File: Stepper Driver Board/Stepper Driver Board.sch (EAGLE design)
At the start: 23 parts, among them IC1 DRV8825PWP

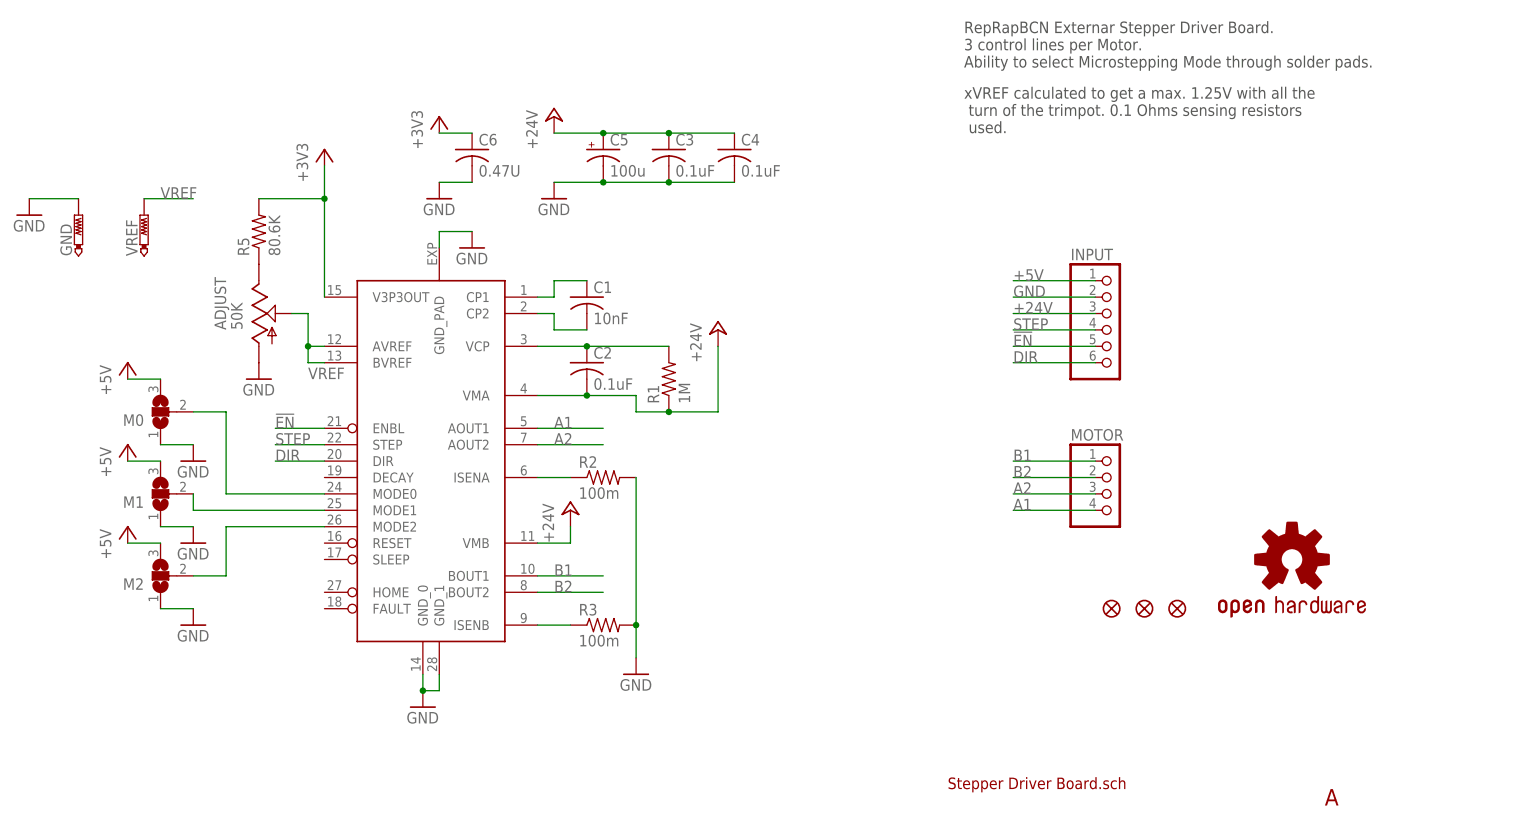
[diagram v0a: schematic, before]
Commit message: The new REV_B has been shipped to production
New MainBoard Design, new Stepper drivers and new Extruder Board.
We also added many new components and configurations
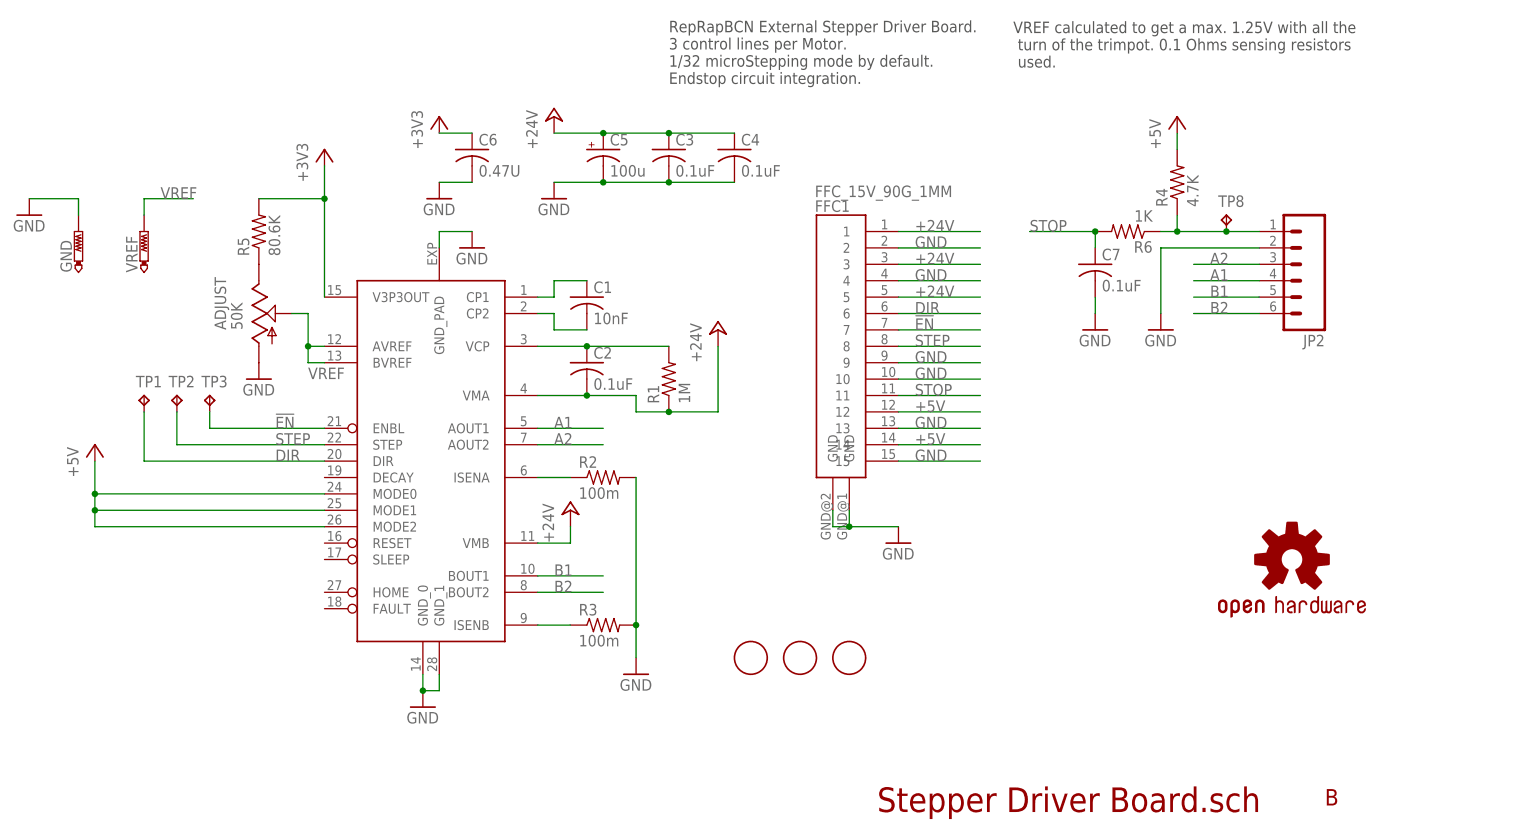
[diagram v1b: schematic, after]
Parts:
- removed FID1, FID2, FID3: FIDUCIAL1X2, SparkFun-Aesthetics:FIDUCIAL1X2
- removed INPUT: (no value), pinhead:PINHD-1X6/90
- removed M0, M1, M2: (no value), jumper:SJ2W
- removed MOTOR: (no value), pinhead:PINHD-1X4/90
- added C7: 0.1uF, rcl:C-USC0805
- added FFC1: FFC_15V_90G_1MM, MarcEagleParts:FFC_15V_90G_1MM
- added JP2: (no value), SparkFun-Connectors:M06SMD
- added R4: 4.7K, rcl:R-US_R0805
- added R6: 1K, rcl:R-US_R0805
- added TP1, TP2, TP3, TP8: TPB1,27, testpad:TPB1,27
- added U$2, U$3, U$4: FIDUCIAL, adafruit:FIDUCIAL
- C5: device rcl:CPOL-USUD-8X10 -> rcl:CPOL-USUD-6,3X7,7
- GND, VREF: value TESTPAD_PTR1TP20SQ -> PTR1TP12R; device SAV MK-I:TESTPAD_PTR1TP20SQ -> testpad:PTR1TP12R; OC_FARNELL unknown -> (none)
- R2, R3: device rcl:R-US_R0805 -> rcl:R-US_R1210
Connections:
- removed net N$10: IC1.MODE1, M1.2
- removed net N$13: IC1.MODE2, M2.2
- removed net N$9: IC1.MODE0, M0.2
- new net N$25: JP2.1, R4.1, R6.1, TP8.TP
- new net N$30: JP2.2
- new net STOP: C7.1, FFC1.11, R6.2
- net !EN: now also FFC1.7, TP3.TP; no longer INPUT.5
- net +24V: now also FFC1.1, FFC1.3, FFC1.5; no longer INPUT.3
- net +5V: now also FFC1.12, FFC1.14, IC1.MODE0, IC1.MODE1, IC1.MODE2, R4.2; no longer INPUT.1, M0.3, M1.3, M2.3
- net A1: now also JP2.4; no longer MOTOR.4
- net A2: now also JP2.3; no longer MOTOR.3
- net B1: now also JP2.5; no longer MOTOR.1
- net B2: now also JP2.6; no longer MOTOR.2
- net DIR: now also FFC1.6, TP1.TP; no longer INPUT.6
- net GND: now also C7.2, FFC1.10, FFC1.13, FFC1.15, FFC1.2, FFC1.4, FFC1.9, FFC1.GND@1, FFC1.GND@2; no longer INPUT.2, M0.1, M1.1, M2.1
- net STEP: now also FFC1.8, TP2.TP; no longer INPUT.4
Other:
- note added: "B"
- note added: "RepRapBCN External Stepper Driver Board. 3 control lines per Motor. 1/32 microStepping mode by default. Endstop circuit integration."
- note added: "VREF calculated to get a max. 1.25V with all the turn of the trimpot. 0.1 Ohms sensing resistors used."
- note removed: "A"
- note removed: "RepRapBCN Externar Stepper Driver Board. 3 control lines per Motor. Ability to select Microstepping Mode through solder pads."
- note removed: "xVREF calculated to get a max. 1.25V with all the turn of the trimpot. 0.1 Ohms sensing resistors used."
- moved on the sheet: GND, VREF

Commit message: BCN3D Electronics REV.E tested and manufactured
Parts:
- removed FFC1: FFC_15V_90G_1MM, MarcEagleParts:FFC_15V_90G_1MM
- removed GND, VREF: PTR1TP12R, testpad:PTR1TP12R
- removed JP2: (no value), SparkFun-Connectors:M06SMD
- removed LOGO1: OSHW-LOGOL, SparkFun-Aesthetics:OSHW-LOGOL
- removed TP8: TPB1,27, testpad:TPB1,27
- added C8: 0.1uF, rcl:C-USC0805
- added FFC2: FFC_15V_90G_1MM, MarcEagleParts:FFC_15V_90G_1MM
- added MOTOR: (no value), MarcEagleParts:M06
- added SMAEX: (no value), SparkFun-Connectors:M03PTH
- added STOP: TPB1,27, testpad:TPB1,27
- added STOP1: (no value), adafruit:JST_2PIN-THM-RA
- added USTEP: (no value), jumper:SJ2W
- !EN, DIR, STEP, U$2, U$3, U$4: OC_FARNELL (none) -> unknown
- C3: value 0.1uF -> 100n
- R4: MF (none) -> PANASONIC ELECTRONIC COMPONENTS; MPN (none) -> ERJP06F4701V; OC_FARNELL (none) -> 1750763
- R6: MF (none) -> BOURNS; MPN (none) -> CR0805-JW-102ELF; OC_FARNELL (none) -> 2008389
- renumbered TP1 to DIR, TP2 to STEP, TP3 to !EN
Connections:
- removed net N$30: JP2.2
- new net N$4: IC1.MODE0, USTEP.2
- net !EN: now also FFC2.9; no longer FFC1.7
- net +24V: now also C8.1, FFC2.11, FFC2.13, FFC2.15; no longer FFC1.1, FFC1.3, FFC1.5
- net +5V: now also FFC2.2, FFC2.4, IC1.RESET, IC1.SLEEP, SMAEX.1, USTEP.3; no longer FFC1.12, FFC1.14, IC1.MODE0, IC1.MODE1
- net A1: now also MOTOR.6; no longer JP2.4
- net A2: now also MOTOR.4; no longer JP2.3
- net B1: now also MOTOR.1; no longer JP2.5
- net B2: now also MOTOR.3; no longer JP2.6
- net DIR: now also FFC2.7; no longer FFC1.6
- net GND: now also C8.2, FFC2.1, FFC2.12, FFC2.14, FFC2.3, FFC2.6, FFC2.8, FFC2.GND@1, FFC2.GND@2, IC1.MODE1, MOTOR.2, MOTOR.5, SMAEX.2, STOP1.2, USTEP.1; no longer FFC1.10, FFC1.13, FFC1.15, FFC1.2, FFC1.4, FFC1.9, FFC1.GND@1, FFC1.GND@2, GND.TP
- net N$25: now also STOP1.1; no longer JP2.1, TP8.TP
- net STEP: now also FFC2.10; no longer FFC1.8
- net STOP: now also FFC2.5, SMAEX.3, STOP.TP; no longer FFC1.11
- net VREF: no longer VREF.TP
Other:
- note added: "BCN3DTechnologies External Stepper Driver Board. 3 control lines per Motor. 1/16 or 1/32 Microstepping configuration throught jumper Endstop circuit integration."
- note added: "D"
- note added: "VREF calculated to get a max. 1.25V with all the turn of the trimpot. 100 mOhms sensing resistors used."
- note removed: "B"
- note removed: "RepRapBCN External Stepper Driver Board. 3 control lines per Motor. 1/32 microStepping mode by default. Endstop circuit integration."
- note removed: "VREF calculated to get a max. 1.25V with all the turn of the trimpot. 0.1 Ohms sensing resistors used."
- moved on the sheet: C4, C7, R4, R6
